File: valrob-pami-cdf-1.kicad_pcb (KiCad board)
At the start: 4 copper layers, 58 x 50 mm, 139 parts, among them J1 Conn_01x04, J2 USB_C_Receptacle_USB2.0_14P, J3 Conn_01x02, J4 Conn_01x04_Pin, J5 Conn_01x06, M1 Motor_Servo, M2 Stepper_Motor_bipolar, M3 Stepper_Motor_bipolar, Q1 Q_NMOS, Q2 Q_NMOS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

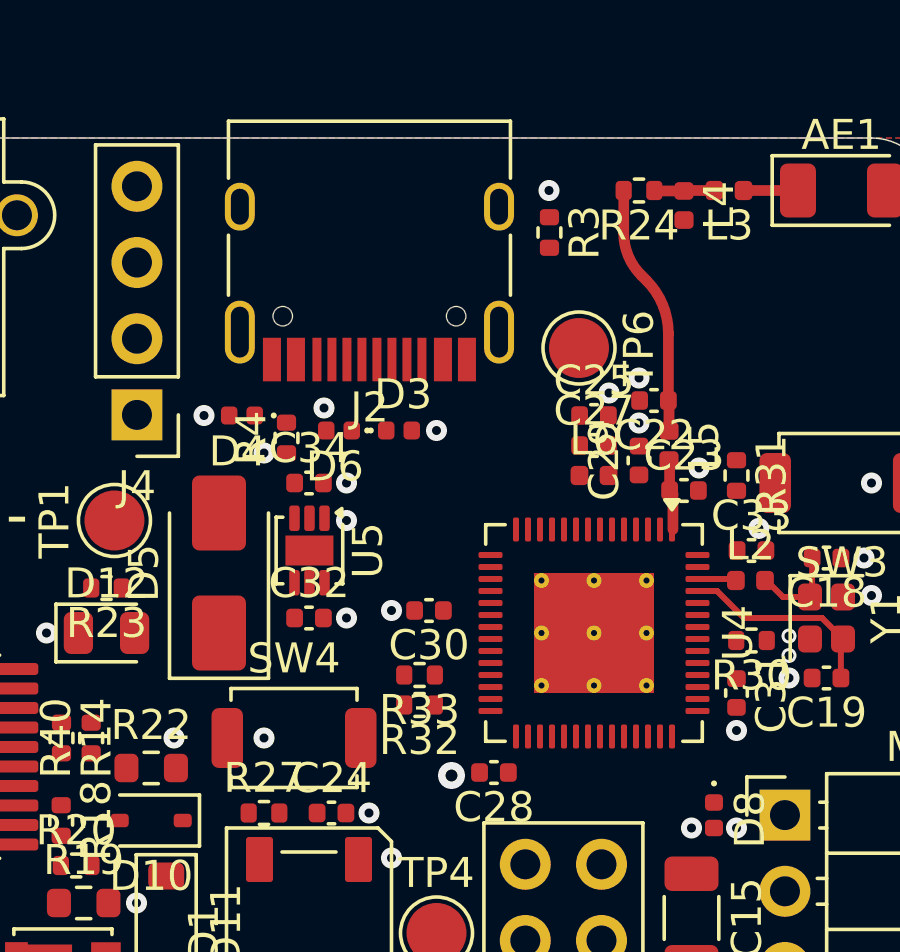
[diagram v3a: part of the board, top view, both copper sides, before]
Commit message: pcb: add usb routing
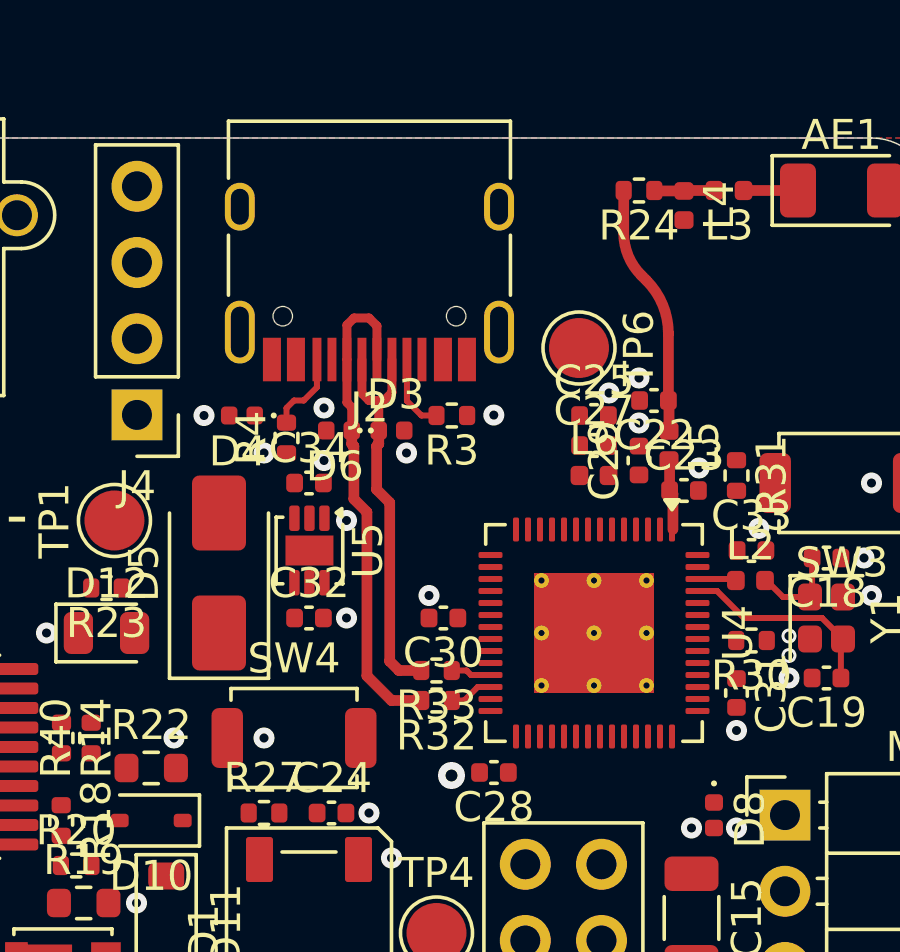
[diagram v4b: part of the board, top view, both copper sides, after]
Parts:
- moved R3 6.91 mm to (164.0, 82.2), turned to 180 degrees
- moved R32 0.58 mm to (163.5, 91.8)
- moved R33 0.58 mm to (163.5, 90.8)
- moved C30 0.54 mm to (163.7, 89.0)
- moved D3 0.25 mm to (162.0, 82.8)
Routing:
- net D+: track 0.00 -> 16.4 mm
- net D-: track 0.00 -> 13.5 mm
- net Net-(J2-CC2): track 0.00 -> 2.72 mm
- net Net-(J2-CC1): track 0.00 -> 2.57 mm
- net /ESP_D-: track 0.00 -> 1.56 mm
- net /ESP_D+: track 0.00 -> 1.48 mm

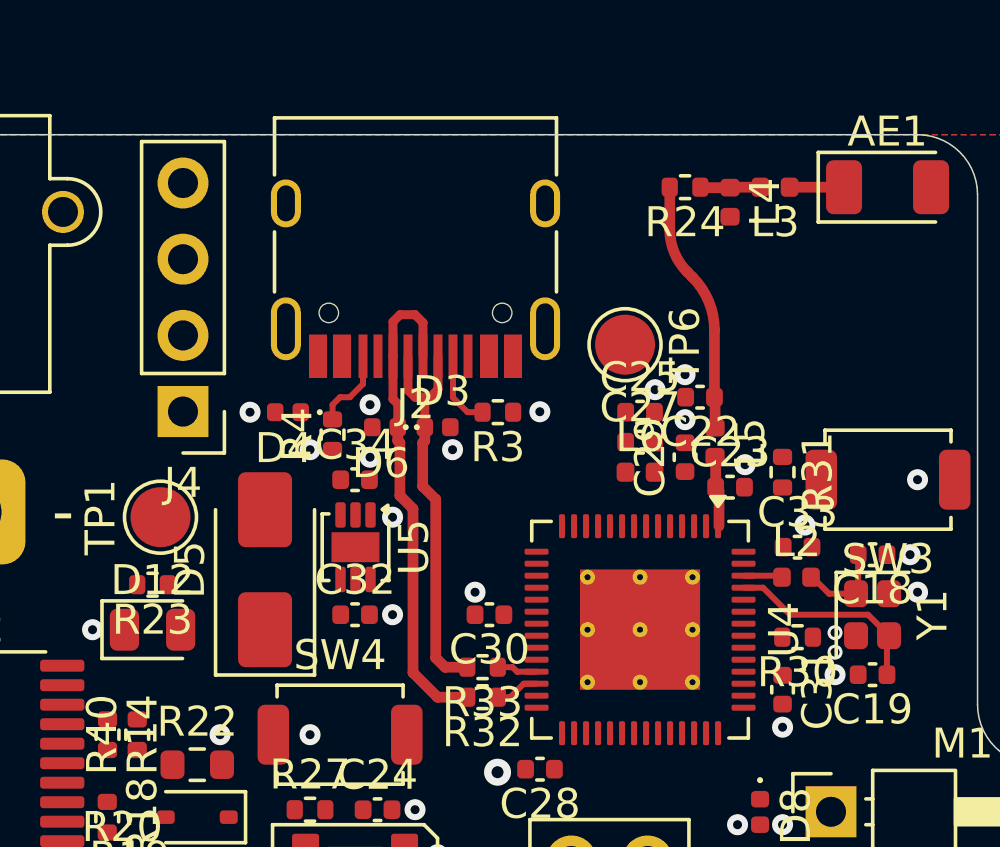
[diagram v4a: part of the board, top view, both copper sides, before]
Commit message: pcb: add uart routing
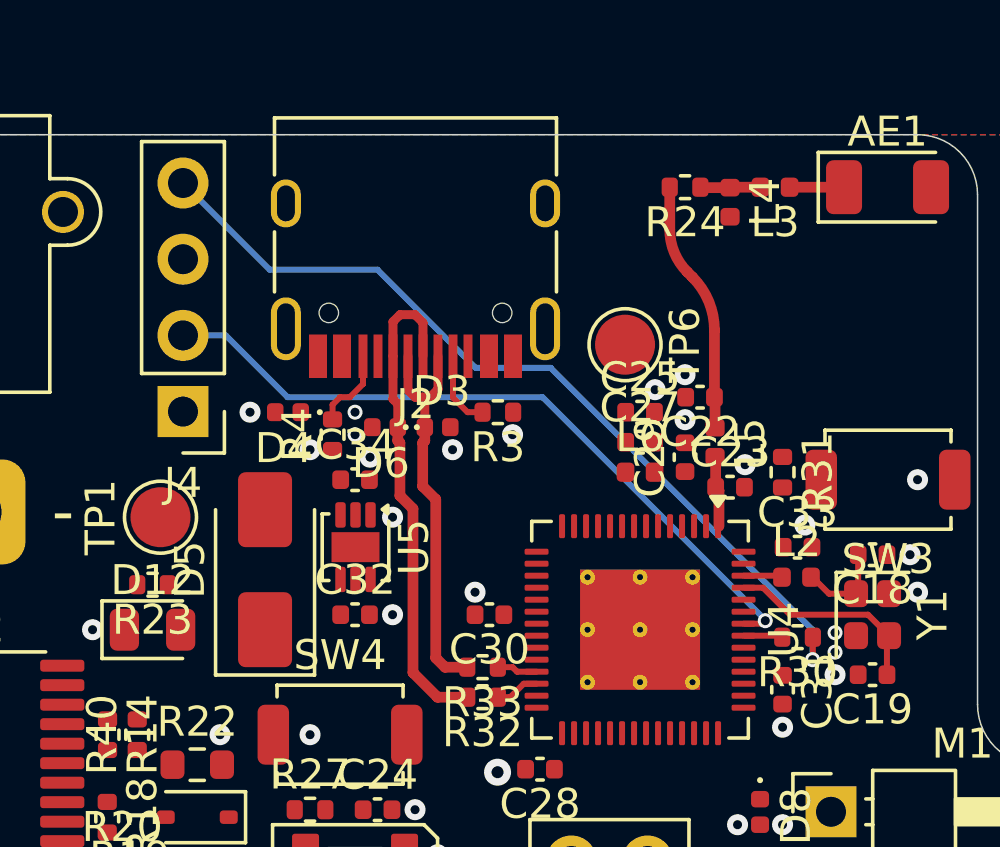
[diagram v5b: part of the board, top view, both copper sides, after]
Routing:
- net Net-(J4-Pin_4): track 0.00 -> 28.9 mm, vias 0 -> 1
- net /U0RXD: track 0.00 -> 24.1 mm, vias 0 -> 1
- net /U0TXD: track 0.00 -> 1.31 mm
- net GND: vias 97 -> 98
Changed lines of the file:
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@@
+	)
+	(via
+		(at 159.25 82.25)
+		(size 0.5)
+		(drill 0.3)
+		(layers "F.Cu" "B.Cu")
+		(free yes)
+		(net 4)
 	)
 	(via
@@
 	)
 	(via
-		(at 165.41 82.235)
+		(at 164.5 83)
 		(size 0.7)
 		(drill 0.3)
@@
 		(at 178 88.25)
 		(size 0.7)
+		(drill 0.3)
+		(layers "F.Cu" "B.Cu")
+		(free yes)
+		(net 4)
+	)
+	(via
+		(at 159.25 83)
+		(size 0.5)
 		(drill 0.3)
 		(layers "F.Cu" "B.Cu")
@@
 	(via
 		(at 163.25 88.25)
-		(size 0.7)
-		(drill 0.3)
-		(layers "F.Cu" "B.Cu")
-		(free yes)
-		(net 4)
-	)
-	(via
-		(at 159.75 82)
 		(size 0.7)
 		(drill 0.3)
@@
 	)
 	(segment
+		(start 172.924165 89.2)
+		(end 172.924165 89.234992)
+		(width 0.2)
+		(layer "F.Cu")
+		(net 50)
+	)
+	(segment
+		(start 172.924165 89.234992)
+		(end 172.859157 89.3)
+		(width 0.2)
+		(layer "F.Cu")
+		(net 50)
+	)
+	(segment
+		(start 172.859157 89.3)
+		(end 172.2 89.3)
+		(width 0.2)
+		(layer "F.Cu")
+		(net 50)
+	)
+	(via
+		(at 172.924165 89.2)
+		(size 0.5)
+		(drill 0.3)
+		(layers "F.Cu" "B.Cu")
+		(net 50)
+	)
+	(segment
+		(start 154.94 79.69)
+		(end 153.515 79.69)
+		(width 0.2)
+		(layer "B.Cu")
+		(net 50)
+	)
+	(segment
+		(start 157 81.75)
+		(end 154.94 79.69)
+		(width 0.2)
+		(layer "B.Cu")
+		(net 50)
+	)
+	(segment
+		(start 172.924165 89.174165)
+		(end 165.5 81.75)
+		(width 0.2)
+		(layer "B.Cu")
+		(net 50)
+	)
+	(segment
+		(start 165.5 81.75)
+		(end 157 81.75)
+		(width 0.2)
+		(layer "B.Cu")
+		(net 50)
+	)
+	(segment
+		(start 172.924165 89.2)
+		(end 172.924165 89.174165)
+		(width 0.2)
+		(layer "B.Cu")
+		(net 50)
+	)
+	(segment
+		(start 174.51 89.75)
+		(end 174.51 90.49)
+		(width 0.2)
+		(layer "F.Cu")
+		(net 51)
+	)
+	(segment
+		(start 174.51 90.49)
+		(end 174.5 90.5)
+		(width 0.2)
+		(layer "F.Cu")
+		(net 51)
+	)
+	(via
+		(at 174.5 90.5)
+		(size 0.5)
+		(drill 0.3)
+		(layers "F.Cu" "B.Cu")
+		(net 51)
+	)
+	(segment
+		(start 156.405 77.5)
+		(end 160 77.5)
+		(width 0.2)
+		(layer "B.Cu")
+		(net 51)
+	)
+	(segment
+		(start 174.5 89.5)
+		(end 174.5 90.5)
+		(width 0.2)
+		(layer "B.Cu")
+		(net 51)
+	)
+	(segment
+		(start 165.771 80.771)
+		(end 174.5 89.5)
+		(width 0.2)
+		(layer "B.Cu")
+		(net 51)
+	)
+	(segment
+		(start 153.515 74.61)
+		(end 156.405 77.5)
+		(width 0.2)
+		(layer "B.Cu")
+		(net 51)
+	)
+	(segment
+		(start 163.271 80.771)
+		(end 165.771 80.771)
+		(width 0.2)
+		(layer "B.Cu")
+		(net 51)
+	)
+	(segment
+		(start 160 77.5)
+		(end 163.271 80.771)
+		(width 0.2)
+		(layer "B.Cu")
+		(net 51)
+	)
+	(segment
 		(start 173.43 87.7)
 		(end 173.48 87.75)
@@
 	)
 	(segment
+		(start 173.44 89.7)
+		(end 173.49 89.75)
+		(width 0.2)
+		(layer "F.Cu")
+		(net 77)
+	)
+	(segment
+		(start 172.2 89.7)
+		(end 173.44 89.7)
+		(width 0.2)
+		(layer "F.Cu")
+		(net 77)
+	)
+	(segment

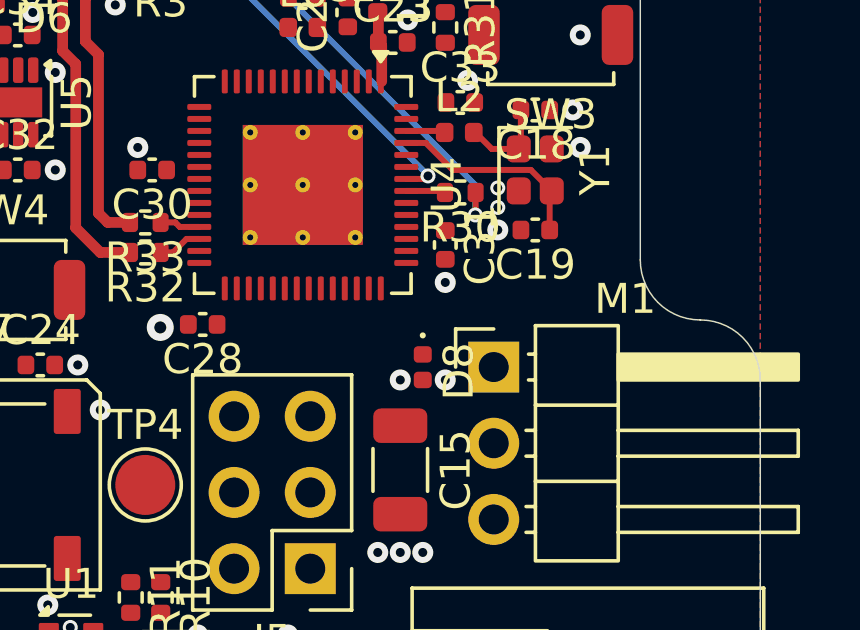
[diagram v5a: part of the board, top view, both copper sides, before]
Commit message: pcb: add servo connector routing
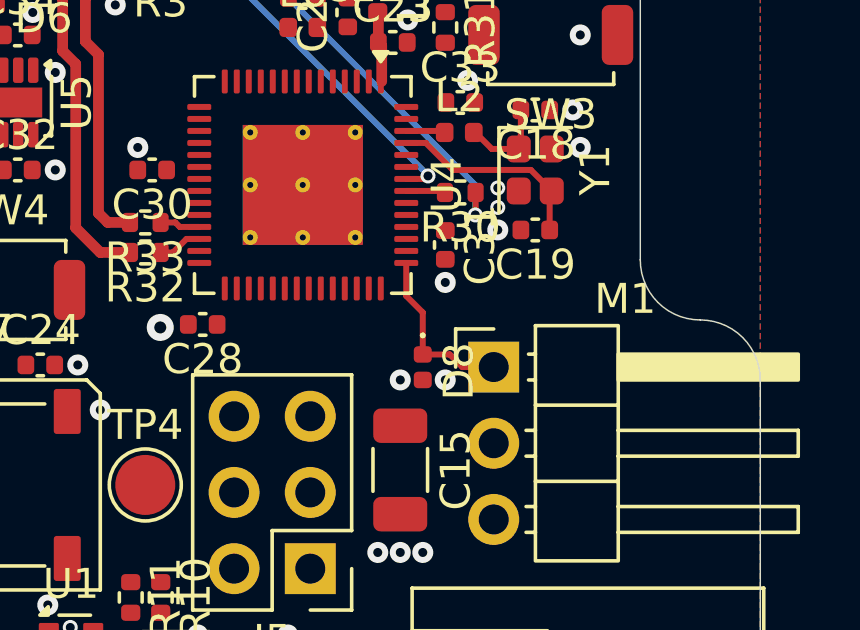
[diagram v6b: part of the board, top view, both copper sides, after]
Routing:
- net /SERVO1: track 0.00 -> 5.82 mm
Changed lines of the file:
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@@
+	)
+	(segment
+		(start 173.65 95.15)
+		(end 172.75 95.15)
+		(width 0.2)
+		(layer "F.Cu")
+		(net 54)
+	)
+	(segment
+		(start 172.2 93.2)
+		(end 172.2 92.1)
+		(width 0.2)
+		(layer "F.Cu")
+		(net 54)
+	)
+	(segment
+		(start 172.75 93.75)
+		(end 172.2 93.2)
+		(width 0.2)
+		(layer "F.Cu")
+		(net 54)
+	)
+	(segment
+		(start 175.115 95.57)
+		(end 174.07 95.57)
+		(width 0.2)
+		(layer "F.Cu")
+		(net 54)
+	)
+	(segment
+		(start 172.75 95.15)
+		(end 172.75 93.75)
+		(width 0.2)
+		(layer "F.Cu")
+		(net 54)
+	)
+	(segment
+		(start 174.07 95.57)
+		(end 173.65 95.15)
+		(width 0.2)
+		(layer "F.Cu")
+		(net 54)
 	)
 	(segment

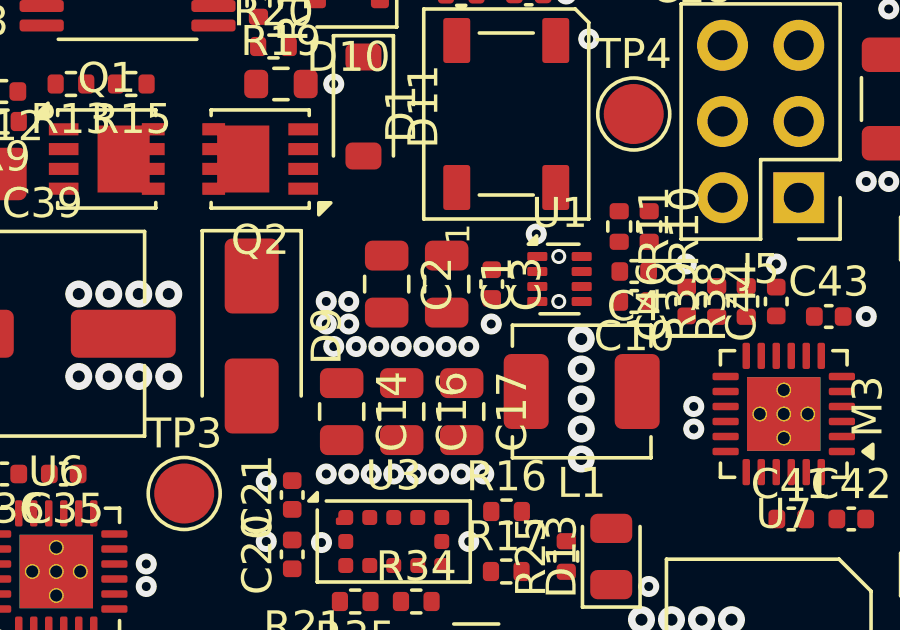
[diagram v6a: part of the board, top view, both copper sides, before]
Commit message: pcb: add smps routing
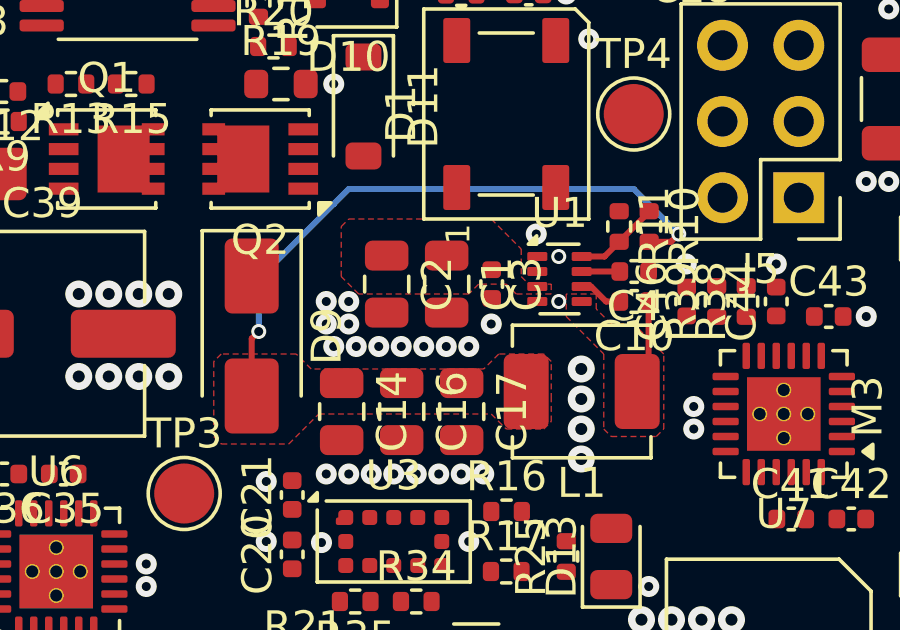
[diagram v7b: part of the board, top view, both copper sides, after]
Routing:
- net +5V: track 0.00 -> 21.0 mm, vias 0 -> 2
- net Net-(U1-SW): track 0.00 -> 3.16 mm
- net Net-(U1-FB): track 0.00 -> 2.89 mm
- net Net-(U1-BST): track 0.00 -> 1.48 mm
- net Net-(U1-SS): track 0.00 -> 1.27 mm
- net GND: vias 98 -> 97
- added copper zone on F.Cu, net +5V
- added copper zone on F.Cu, net +BATT
- added copper zone on F.Cu, net Net-(U1-SW)
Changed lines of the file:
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@@
 			(pinfunction "RT")
 			(pintype "passive")
+			(zone_connect 2)
 			(thermal_bridge_angle 45)
 		)
@@
 			(pinfunction "GND")
 			(pintype "power_in")
+			(zone_connect 2)
 			(thermal_bridge_angle 45)
 		)
@@
 	)
 	(via
-		(at 161.75 107)
-		(size 0.9)
-		(drill 0.4)
-		(layers "F.Cu" "B.Cu")
-		(free yes)
-		(net 4)
-	)
-	(via
 		(at 164.5 83)
 		(size 0.7)
@@
 	)
 	(segment
+		(start 163.035 104.75)
+		(end 161.765 104.75)
+		(width 0.2)
+		(layer "F.Cu")
+		(net 6)
+	)
+	(segment
+		(start 162.077064 105.25)
+		(end 161.765 105.25)
+		(width 0.2)
+		(layer "F.Cu")
+		(net 13)
+	)
+	(segment
+		(start 163.035 105.75)
+		(end 162.577064 105.75)
+		(width 0.2)
+		(layer "F.Cu")
+		(net 13)
+	)
+	(segment
+		(start 162.577064 105.75)
+		(end 162.077064 105.25)
+		(width 0.2)
+		(layer "F.Cu")
+		(net 13)
+	)
+	(segment
+		(start 163.995 105.75)
+		(end 163.995 108.37)
+		(width 0.2)
+		(layer "F.Cu")
+		(net 14)
+	)
+	(segment
+		(start 163.995 108.37)
+		(end 163.615 108.75)
+		(width 0.2)
+		(layer "F.Cu")
+		(net 14)
+	)
+	(segment
+		(start 164.74 103.76)
+		(end 164.015 103.76)
+		(width 0.2)
+		(layer "F.Cu")
+		(net 17)
+	)
+	(segment
+		(start 150.765 106.985)
+		(end 151 106.75)
+		(width 0.2)
+		(layer "F.Cu")
+		(net 17)
+	)
+	(segment
+		(start 165 103.5)
+		(end 164.74 103.76)
+		(width 0.2)
+		(layer "F.Cu")
+		(net 17)
+	)
+	(segment
+		(start 150.765 108.9)
+		(end 150.765 106.985)
+		(width 0.2)
+		(layer "F.Cu")
+		(net 17)
+	)
+	(via
+		(at 151 106.75)
+		(size 0.5)
+		(drill 0.3)
+		(layers "F.Cu" "B.Cu")
+		(net 17)
+	)
+	(via
+		(at 165 103.5)
+		(size 0.5)
+		(drill 0.3)
+		(layers "F.Cu" "B.Cu")
+		(net 17)
+	)
+	(segment
+		(start 151 105)
+		(end 153.5 102.5)
+		(width 0.2)
+		(layer "B.Cu")
+		(net 17)
+	)
+	(segment
+		(start 163.5 102)
+		(end 165 103.5)
+		(width 0.2)
+		(layer "B.Cu")
+		(net 17)
+	)
+	(segment
+		(start 154 102)
+		(end 159 102)
+		(width 0.2)
+		(layer "B.Cu")
+		(net 17)
+	)
+	(segment
+		(start 151 106.75)
+		(end 151 105)
+		(width 0.2)
+		(layer "B.Cu")
+		(net 17)
+	)
+	(segment
+		(start 153.5 102.5)
+		(end 154 102)
+		(width 0.2)
+		(layer "B.Cu")
+		(net 17)
+	)
+	(segment
+		(start 159 102)
+		(end 163.5 102)
+		(width 0.2)
+		(layer "B.Cu")
+		(net 17)
+	)
+	(segment
 		(start 174.5 87.75)
 		(end 175.05 88.3)
@@
 	)
 	(segment
+		(start 164.015 102.74)
+		(end 164.015 102.76)
+		(width 0.2)
+		(layer "F.Cu")
+		(net 68)
+	)
+	(segment
+		(start 162.525 104.25)
+		(end 163.015 103.76)
+		(width 0.2)
+		(layer "F.Cu")
+		(net 68)
+	)
+	(segment
+		(start 161.765 104.25)
+		(end 162.525 104.25)
+		(width 0.2)
+		(layer "F.Cu")
+		(net 68)
+	)
+	(segment
+		(start 164.015 102.76)
+		(end 163.015 103.76)
+		(width 0.2)
+		(layer "F.Cu")
+		(net 68)
+	)
+	(segment
 		(start 173.44 89.7)
 		(end 173.49 89.75)
@@
 	)
 	(zone
+		(net 14)
+		(net_name "Net-(U1-SW)")
+		(layer "F.Cu")
+		(hatch edge 0.5)
+		(priority 3)
+		(connect_pads yes
+			(clearance 0.2)
+		)
+		(min_thickness 0.15)
+		(filled_areas_thickness no)
+		(fill yes
+			(thermal_gap 0.35)
+			(thermal_bridge_width 0.35)
+		)
+		(polygon
+			(pts
+				(xy 161.25 105.5) (xy 161.25 106.25) (xy 162.5 107.5) (xy 162.5 110) (xy 162.75 110.25) (xy 164.25 110.25)
+				(xy 164.5 110) (xy 164.5 107.5) (xy 163.5 106.5) (xy 162.75 106.5) (xy 162.25 106) (xy 162.25 105.5)
+			)
+		)
+	)
+	(zone
+		(net 5)
+		(net_name "+BATT")
+		(layer "F.Cu")
+		(hatch edge 0.5)
+		(priority 1)
+		(connect_pads yes
+			(clearance 0.2)
+		)
+		(min_thickness 0.15)
+		(filled_areas_thickness no)
+		(fill yes
+			(thermal_gap 0.35)
+			(thermal_bridge_width 0.35)
+		)
+		(polygon
+			(pts
+				(xy 160.75 105.5) (xy 159.58 105.5) (xy 159.25 105.17) (xy 158.33 105.17) (xy 158 105.5) (xy 154.33 105.5)
+				(xy 153.75 104.92) (xy 153.75 103.25) (xy 154 103) (xy 158.75 103) (xy 159.75 104) (xy 159.75 104.92)
+				(xy 160 105.17) (xy 160.75 105.17)
+			)
+		)
+	)
+	(zone
+		(net 17)
+		(net_name "+5V")
+		(layer "F.Cu")
+		(hatch edge 0.5)
+		(priority 2)
+		(connect_pads yes
+			(clearance 0.2)
+		)
+		(min_thickness 0.15)
+		(filled_areas_thickness no)
+		(fill yes
+			(thermal_gap 0.35)
+			(thermal_bridge_width 0.35)
+		)
+		(polygon
+			(pts
+				(xy 160.75 107.75) (xy 160.5 107.5) (xy 159 107.5) (xy 158.5 108) (xy 152.75 108) (xy 152.25 107.5)
+				(xy 149.75 107.5) (xy 149.5 107.75) (xy 149.5 110.25) (xy 149.75 110.5) (xy 152 110.5) (xy 153 109.5)
+				(xy 158.75 109.5) (xy 159.25 110) (xy 160.5 110) (xy 160.75 109.75) (xy 160.75 109)
+			)
+		)
+	)
+	(zone
